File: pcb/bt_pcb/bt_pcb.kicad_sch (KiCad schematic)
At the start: 0 parts

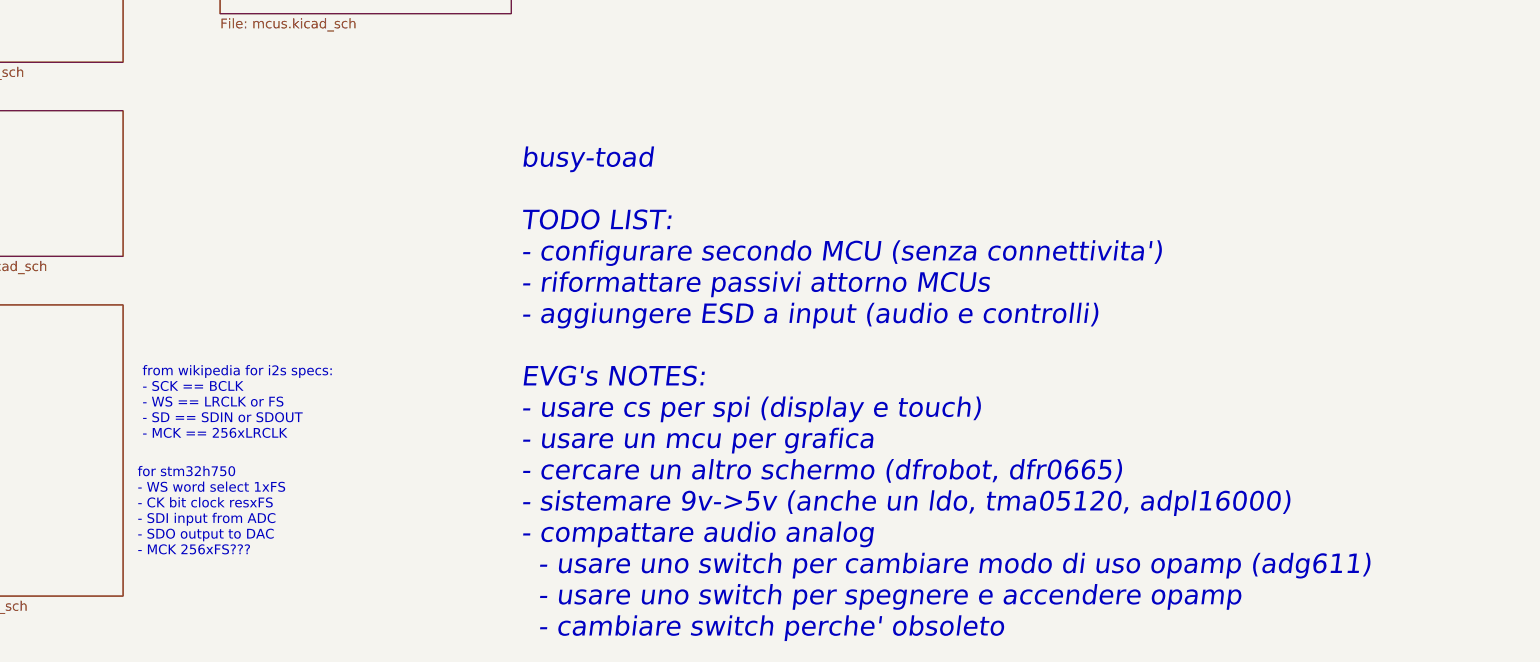
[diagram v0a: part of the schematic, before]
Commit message: ditching power pcb, new codec
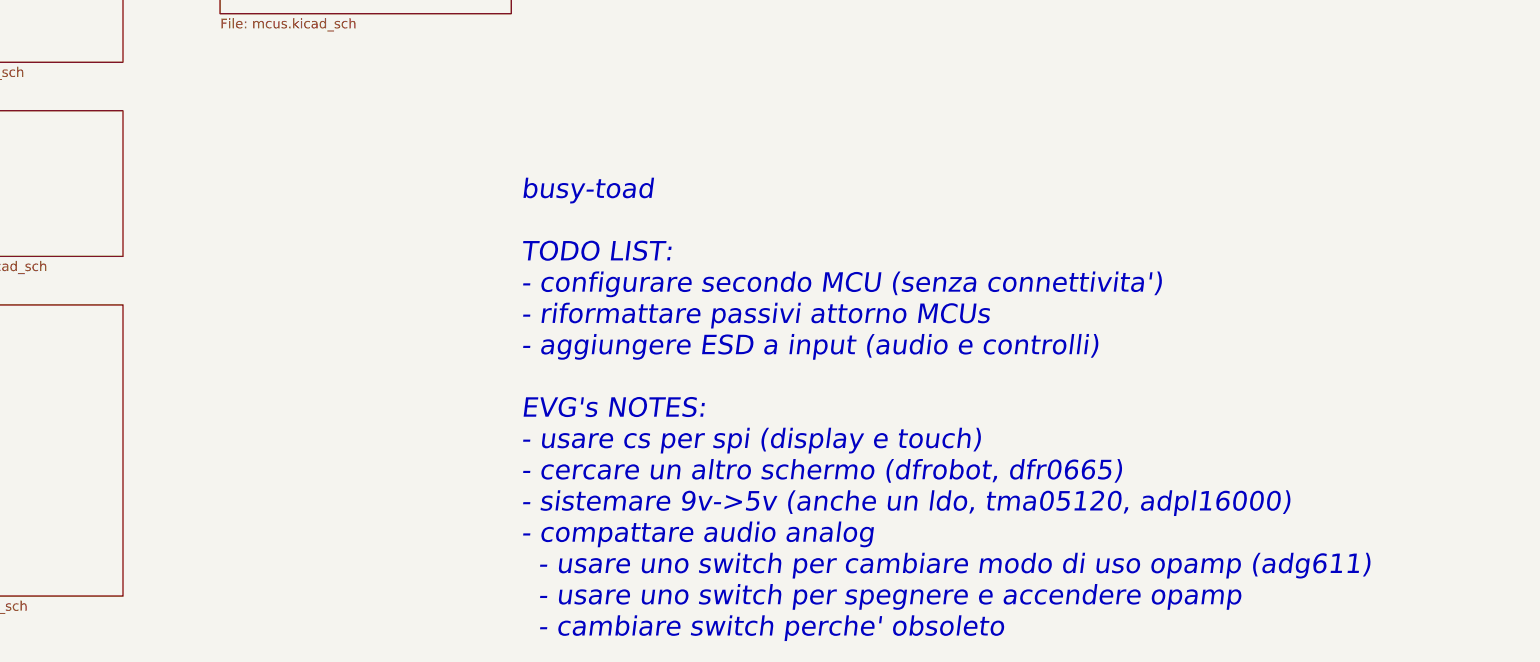
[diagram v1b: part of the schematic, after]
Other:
- note added: "busy-toad TODO LIST: - configurare secondo MCU (senza connettivita') - riformattare passivi attorno MCUs - aggiungere ESD a input (audio e controlli) EVG's NOTES: - usare cs per spi (display e touch) - cercare un altro schermo (dfrobot, dfr0665) - sistemare 9v->5v (anche un ldo, tma05120, adpl16000) - compattare audio analog - usare uno switch per cambiare modo di uso opamp (adg611) - usare uno s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"
- note removed: "busy-toad TODO LIST: - configurare secondo MCU (senza connettivita') - riformattare passivi attorno MCUs - aggiungere ESD a input (audio e controlli) EVG's NOTES: - usare cs per spi (display e touch) - usare un mcu per grafica - cercare un altro schermo (dfrobot, dfr0665) - sistemare 9v->5v (anche un ldo, tma05120, adpl16000) - compattare audio analog - usare uno switch per cambiare modo di uso o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"
- note removed: "for stm32h750 - WS word select 1xFS - CK bit clock resxFS - SDI input from ADC - SDO output to DAC - MCK 256xFS???"
- note removed: "from wikipedia for i2s specs: - SCK == BCLK - WS == LRCLK or FS - SD == SDIN or SDOUT - MCK == 256xLRCLK"

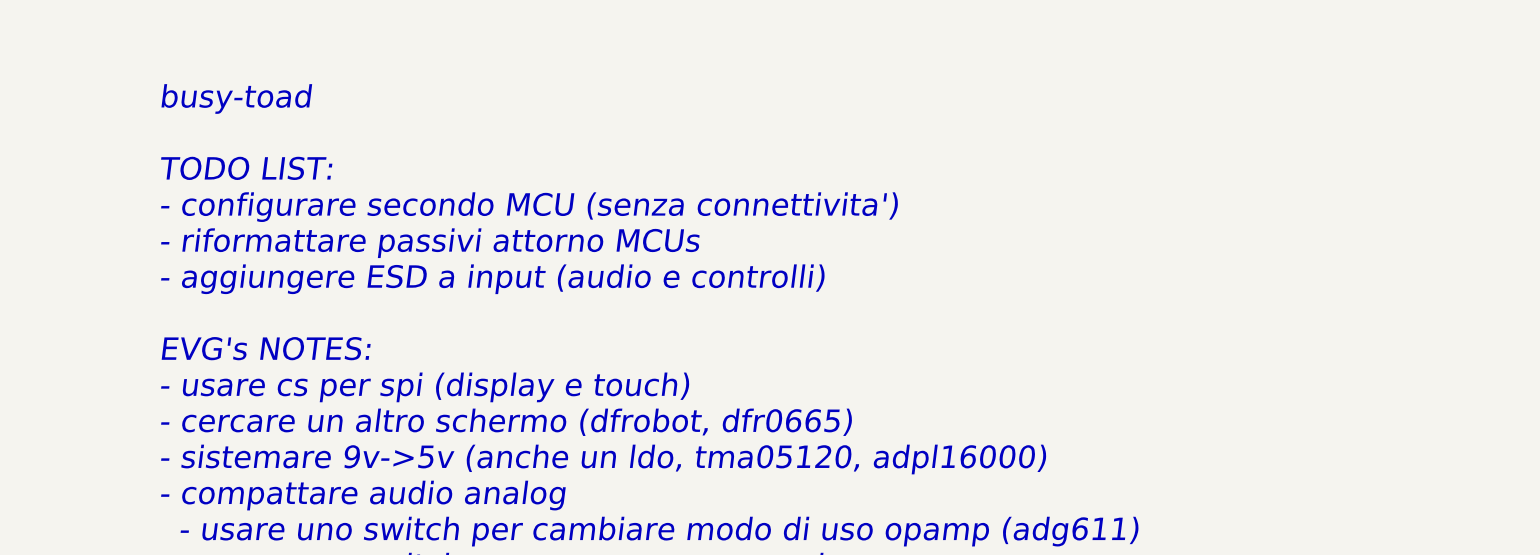
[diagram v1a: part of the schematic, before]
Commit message: complete makeover of power supply
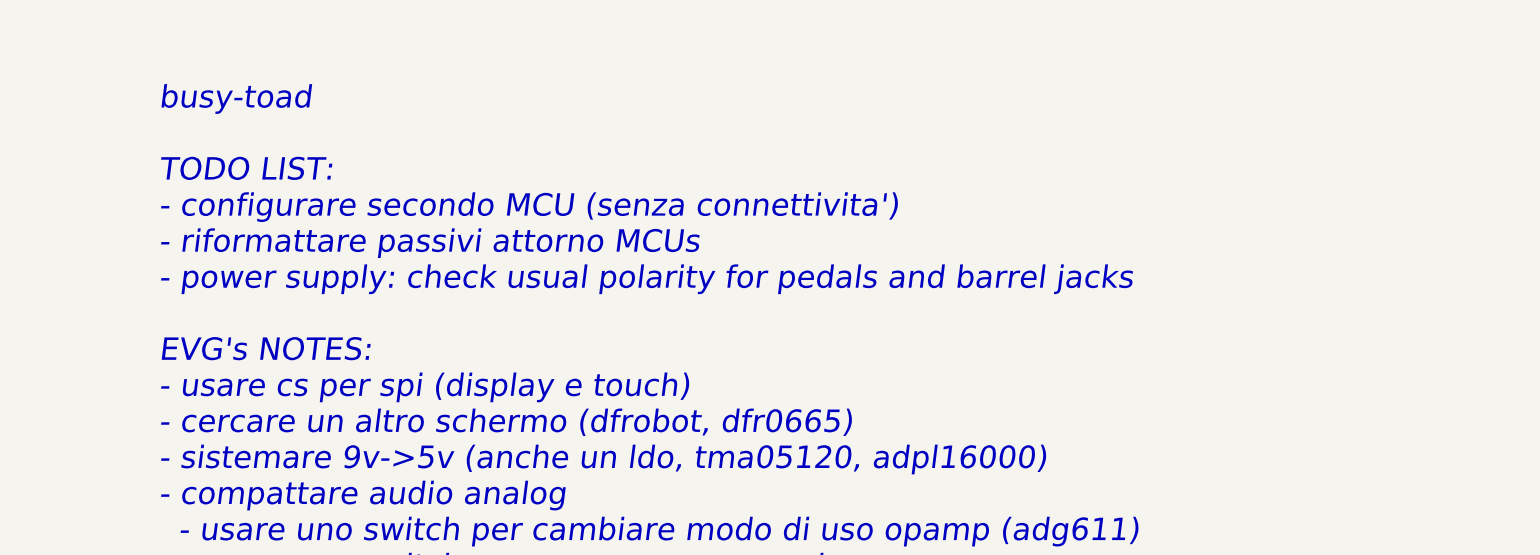
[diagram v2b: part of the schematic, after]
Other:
- note added: "busy-toad TODO LIST: - configurare secondo MCU (senza connettivita') - riformattare passivi attorno MCUs - power supply: check usual polarity for pedals and barrel jacks EVG's NOTES: - usare cs per spi (display e touch) - cercare un altro schermo (dfrobot, dfr0665) - sistemare 9v->5v (anche un ldo, tma05120, adpl16000) - compattare audio analog - usare uno switch per cambiare modo di uso opamp (a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"
- note removed: "busy-toad TODO LIST: - configurare secondo MCU (senza connettivita') - riformattare passivi attorno MCUs - aggiungere ESD a input (audio e controlli) EVG's NOTES: - usare cs per spi (display e touch) - cercare un altro schermo (dfrobot, dfr0665) - sistemare 9v->5v (anche un ldo, tma05120, adpl16000) - compattare audio analog - usare uno switch per cambiare modo di uso opamp (adg611) - usare uno s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"
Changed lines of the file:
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@@
 	(generator_version "9.0")
 	(paper "A4")
-	(text "busy-toad\n\nTODO LIST:\n- configurare secondo MCU (senza connettivita')\n- riformattare passivi attorno MCUs\n- aggiungere ESD a input (audio e controlli)\n\nEVG's NOTES:\n- usare cs per spi (display e touch)\n- cercare un altro schermo (dfrobot, dfr0665)\n- sistemare 9v->5v (anche un ldo, tma05120, adpl16000)\n- compattare audio analog\n  - usare uno switch per cambiare modo di uso opamp (adg611) \n  - usare uno switch per spegnere e accendere opamp\n  - cambiare switch perche' obsoleto\n"
+	(text "busy-toad\n\nTODO LIST:\n- configurare secondo MCU (senza connettivita')\n- riformattare passivi attorno MCUs\n- power supply: check usual polarity for pedals and barrel jacks\n\nEVG's NOTES:\n- usare cs per spi (display e touch)\n- cercare un altro schermo (dfrobot, dfr0665)\n- sistemare 9v->5v (anche un ldo, tma05120, adpl16000)\n- compattare audio analog\n  - usare uno switch per cambiare modo di uso opamp (adg611) \n  - usare uno switch per spegnere e accendere opamp\n  - cambiare switch perche' obsoleto\n"
 		(exclude_from_sim no)
 		(at 115.57 145.415 0)

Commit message: solving some erc warnings and errors
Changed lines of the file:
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@@
 	(text "busy-toad\n\nTODO LIST:\n- configurare secondo MCU (senza connettivita')\n- riformattare passivi attorno MCUs\n- power supply: check usual polarity for pedals and barrel jacks\n\nEVG's NOTES:\n- usare cs per spi (display e touch)\n- cercare un altro schermo (dfrobot, dfr0665)\n- sistemare 9v->5v (anche un ldo, tma05120, adpl16000)\n- compattare audio analog\n  - usare uno switch per cambiare modo di uso opamp (adg611) \n  - usare uno switch per spegnere e accendere opamp\n  - cambiare switch perche' obsoleto\n"
 		(exclude_from_sim no)
-		(at 115.57 145.415 0)
+		(at 115.57 146.05 0)
 		(effects
 			(font

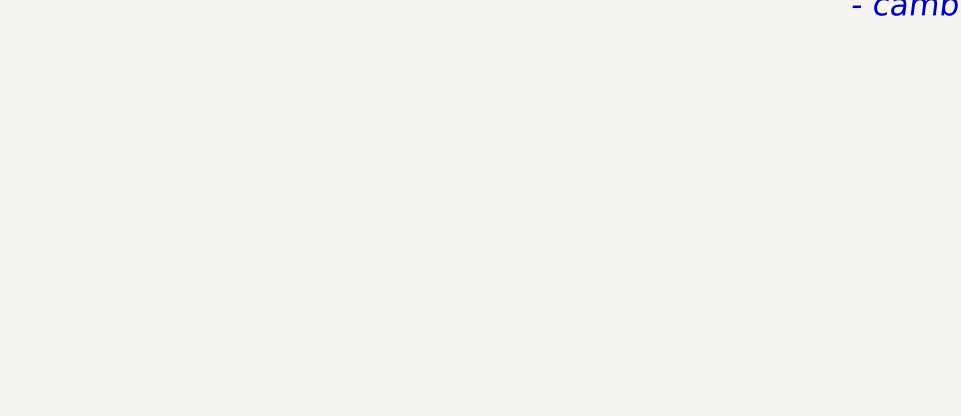
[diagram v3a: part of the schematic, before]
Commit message: pcb with some schematic tuning
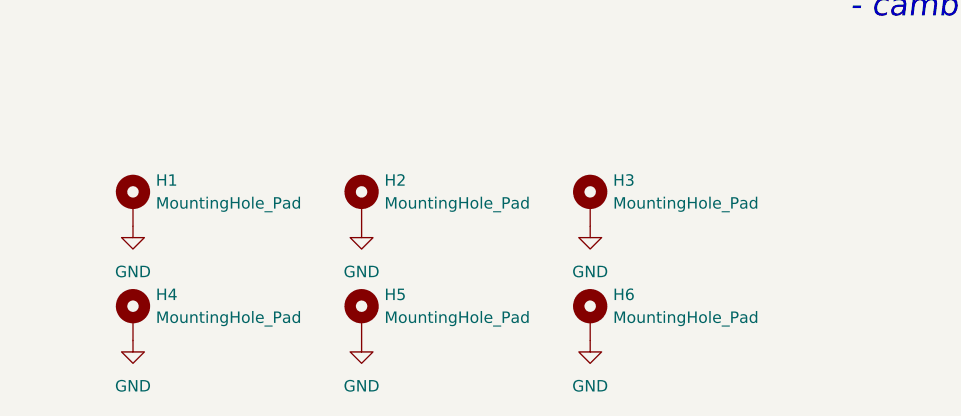
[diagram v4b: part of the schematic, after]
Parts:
- added H1, H2, H3, H4, H5, H6: MountingHole_Pad, MountingHole:MountingHole_3.2mm_M3_ISO14580_Pad, symbol Mechanical:MountingHole_Pad
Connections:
- new net GND: H1.1, H2.1, H3.1, H4.1, H5.1, H6.1

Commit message: continuing review
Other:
- note added: "busy-toad TODO LIST:"
- note removed: "busy-toad TODO LIST: - configurare secondo MCU (senza connettivita') - riformattare passivi attorno MCUs - power supply: check usual polarity for pedals and barrel jacks EVG's NOTES: - usare cs per spi (display e touch) - cercare un altro schermo (dfrobot, dfr0665) - sistemare 9v->5v (anche un ldo, tma05120, adpl16000) - compattare audio analog - usare uno switch per cambiare modo di uso opamp (a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"
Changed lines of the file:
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@@
 	(generator_version "9.0")
 	(paper "A4")
-	(text "busy-toad\n\nTODO LIST:\n- configurare secondo MCU (senza connettivita')\n- riformattare passivi attorno MCUs\n- power supply: check usual polarity for pedals and barrel jacks\n\nEVG's NOTES:\n- usare cs per spi (display e touch)\n- cercare un altro schermo (dfrobot, dfr0665)\n- sistemare 9v->5v (anche un ldo, tma05120, adpl16000)\n- compattare audio analog\n  - usare uno switch per cambiare modo di uso opamp (adg611) \n  - usare uno switch per spegnere e accendere opamp\n  - cambiare switch perche' obsoleto\n"
+	(text "busy-toad\n\nTODO LIST:\n"
 		(exclude_from_sim no)
 		(at 115.57 146.05 0)

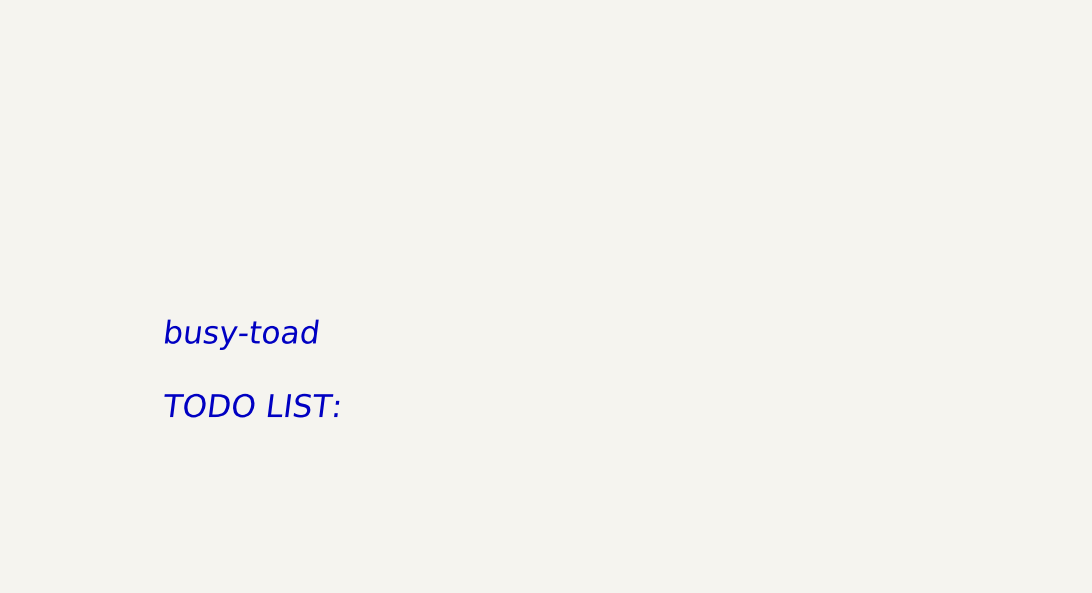
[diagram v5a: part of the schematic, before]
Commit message: layed components down
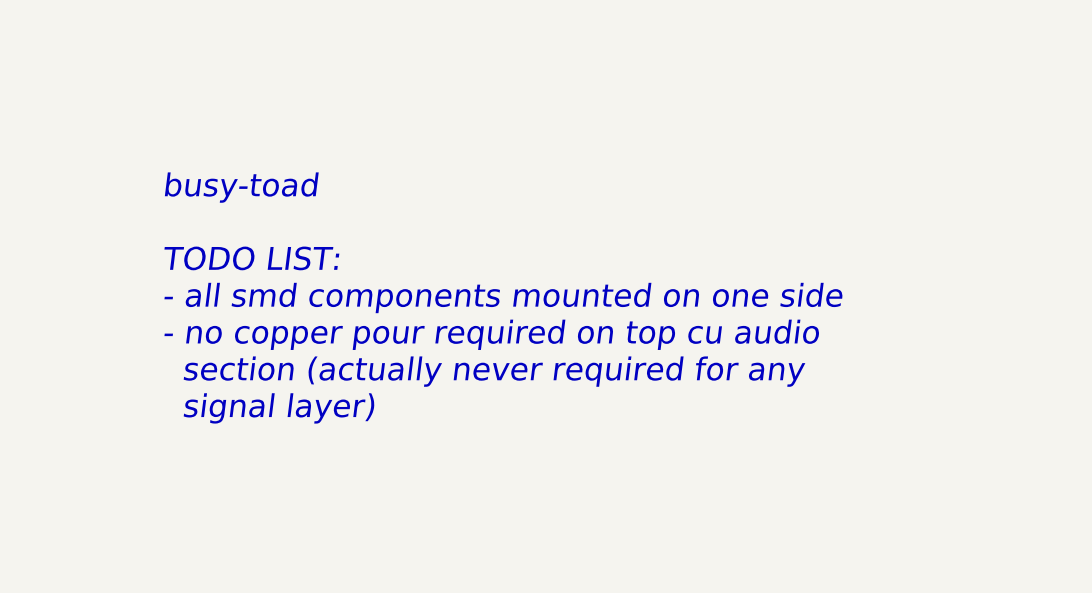
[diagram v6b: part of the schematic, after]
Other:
- note added: "busy-toad TODO LIST: - all smd components mounted on one side - no copper pour required on top cu audio section (actually never required for any signal layer)"
- note removed: "busy-toad TODO LIST:"
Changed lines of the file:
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@@
 	(generator_version "9.0")
 	(paper "A4")
-	(text "busy-toad\n\nTODO LIST:\n"
+	(text "busy-toad\n\nTODO LIST:\n- all smd components mounted on one side\n- no copper pour required on top cu audio\n  section (actually never required for any\n  signal layer)\n"
 		(exclude_from_sim no)
 		(at 115.57 146.05 0)

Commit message: updated and pretty bom
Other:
- note added: "busy-toad TODO LIST:"
- note removed: "busy-toad TODO LIST: - all smd components mounted on one side - no copper pour required on top cu audio section (actually never required for any signal layer)"
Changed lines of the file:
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@@
 	(generator_version "9.0")
 	(paper "A4")
-	(text "busy-toad\n\nTODO LIST:\n- all smd components mounted on one side\n- no copper pour required on top cu audio\n  section (actually never required for any\n  signal layer)\n"
+	(text "busy-toad\n\nTODO LIST:\n"
 		(exclude_from_sim no)
 		(at 115.57 146.05 0)
